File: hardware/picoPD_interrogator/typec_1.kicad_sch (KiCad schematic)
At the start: 26 parts, among them J2 USB_C_Receptacle_USB2.0_16P, Q1 rohm-RE1C002UN, Q2 rohm-RE1C002UN, Q4 rohm-RE1C002UN, Q5 rohm-RE1C002UN, U3 ST-LM393QT, U4 TI_SN74LVC1G3157-Q1, U5 TI_SN74LVC1G3157-Q1

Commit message: Updated schematic/BOM.
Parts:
- R30, R31: DigiKey PN RMCF0201ZT0R00CT-ND -> P122655CT-N; Manufacturer Stackpole Electronics Inc -> Panasonic Electronic Components; Manufacturer PN RMCF0201ZT0R00 -> ERJ-1GNF1003C
- R4, R5: DigiKey PN (none) -> P122955CT-ND; Manufacturer (none) -> Panasonic Industry; Manufacturer PN (none) -> ERJ-1GNF34R8C
- R9: DigiKey PN (none) -> P123051CT-N; Manufacturer (none) -> Panasonic Electronic Components; Manufacturer PN (none) -> ERJ-1GNF5101C

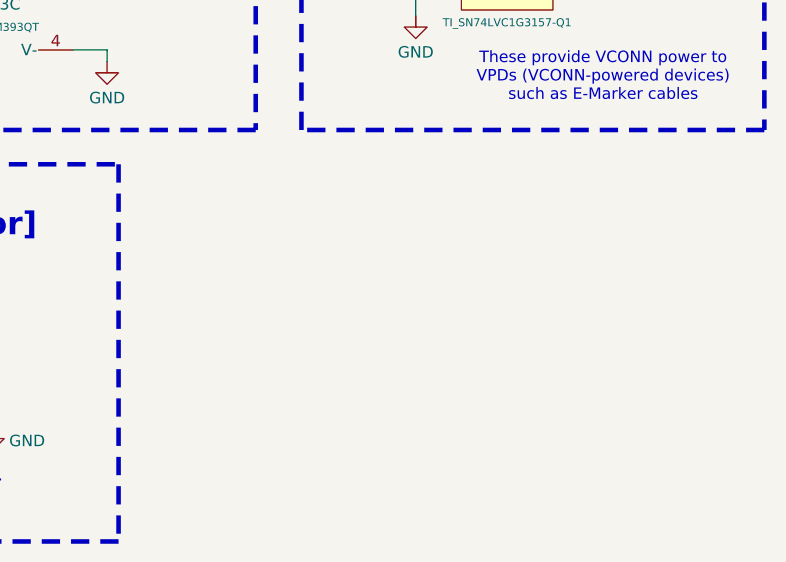
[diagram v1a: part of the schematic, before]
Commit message: Added 5v boost circuit, VBUS feedback to each port.
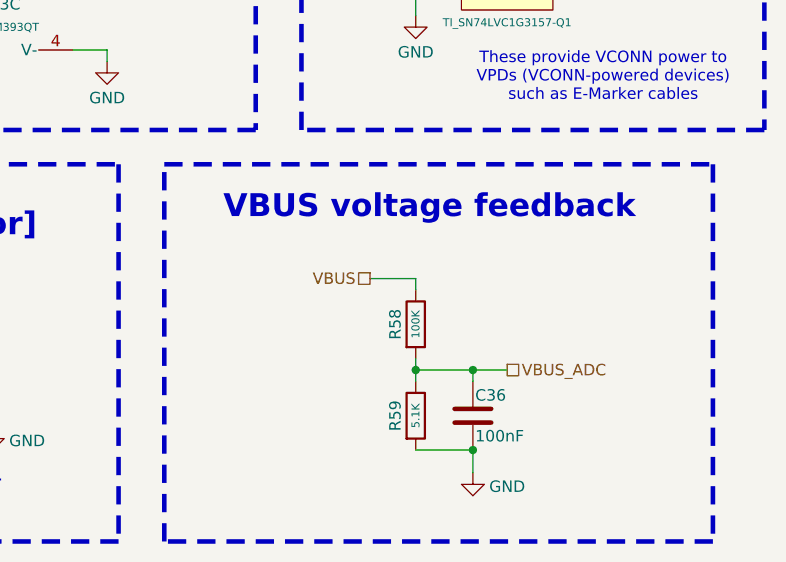
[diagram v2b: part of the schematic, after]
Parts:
- added C36: 100nF, Capacitor_SMD:C_0201_0603Metric, symbol Device:C
- added R58: 100K, Resistor_SMD:R_0201_0603Metric, symbol Device:R
- added R59: 5.1K, Resistor_SMD:R_0201_0603Metric, symbol Device:R
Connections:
- net GND: now also C36.2, R59.2
- net VBUS: now also R58.1
- new net VBUS_ADC: C36.1, R58.2, R59.1
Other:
- note added: "VBUS voltage feedback"

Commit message: Working on CYW43 stuff. Getting ready to test various PCB sizes.
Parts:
- R58: DigiKey PN (none) -> P122655CT-N; Manufacturer (none) -> Panasonic Electronic Components; Manufacturer PN (none) -> ERJ-1GNF1003C
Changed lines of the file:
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@@
 			)
 		)
-		(property "Description" ""
+		(property "Description" "RES SMD 100K OHM 1% 1/20W 0201"
 			(at 110.49 168.91 0)
 			(hide yes)
@@
 			)
 		)
-		(property "Manufacturer" ""
+		(property "Manufacturer" "Panasonic Electronic Components"
 			(at 110.49 168.91 0)
 			(hide yes)
@@
 			)
 		)
-		(property "DigiKey PN" ""
+		(property "DigiKey PN" "P122655CT-N"
 			(at 110.49 168.91 0)
 			(hide yes)
@@
 			)
 		)
-		(property "Manufacturer PN" ""
+		(property "Manufacturer PN" "ERJ-1GNF1003C"
 			(at 110.49 168.91 0)
 			(hide yes)

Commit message: Working on basic layout.
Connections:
- net GND: no longer J2.S1 (SHIELD)
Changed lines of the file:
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@@
-	)
-	(junction
-		(at 115.57 73.66)
-		(diameter 0)
-		(color 0 0 0 0)
 	)
 	(junction
@@
 		(pts
 			(xy 34.29 171.45) (xy 33.02 171.45)
-		)
-		(stroke
-			(width 0)
-			(type default)
-		)
-	)
-	(wire
-		(pts
-			(xy 107.95 73.66) (xy 115.57 73.66)
 		)
 		(stroke
@@
 		(pin "A9"
 		)
-		(pin "S1"
-		)
 		(pin "A1"
